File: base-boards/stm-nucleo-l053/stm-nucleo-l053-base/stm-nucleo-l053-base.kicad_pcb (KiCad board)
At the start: 2 copper layers, 162.6 x 104.8 mm, 18 parts, among them SW1 SW_SPST, SW2 SW_SPST, SW3 SW_SPST, SW4 SW_SPST, U1 NUCLEO-L053R8

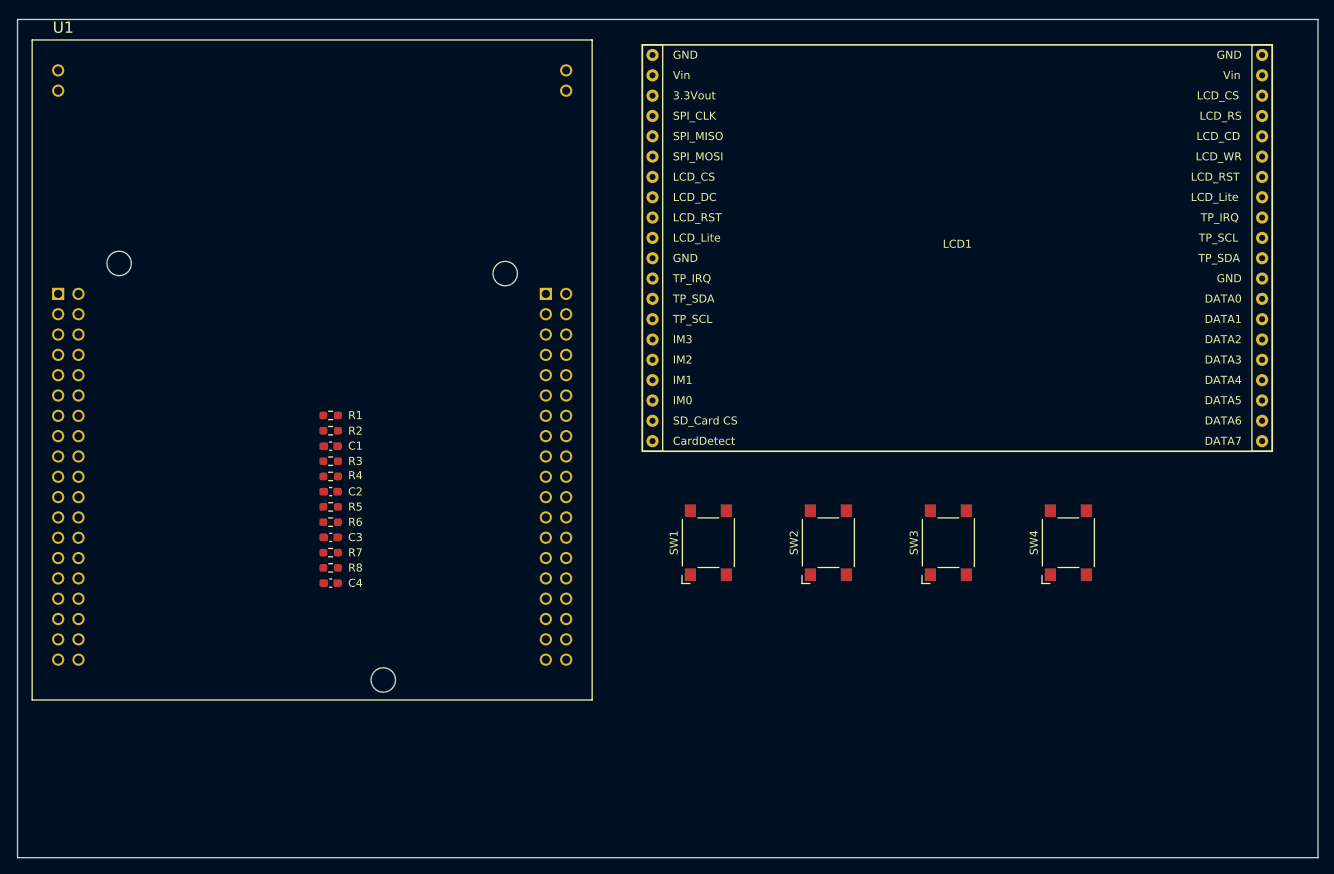
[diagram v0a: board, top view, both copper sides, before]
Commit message: Added Arduino Nano breakout
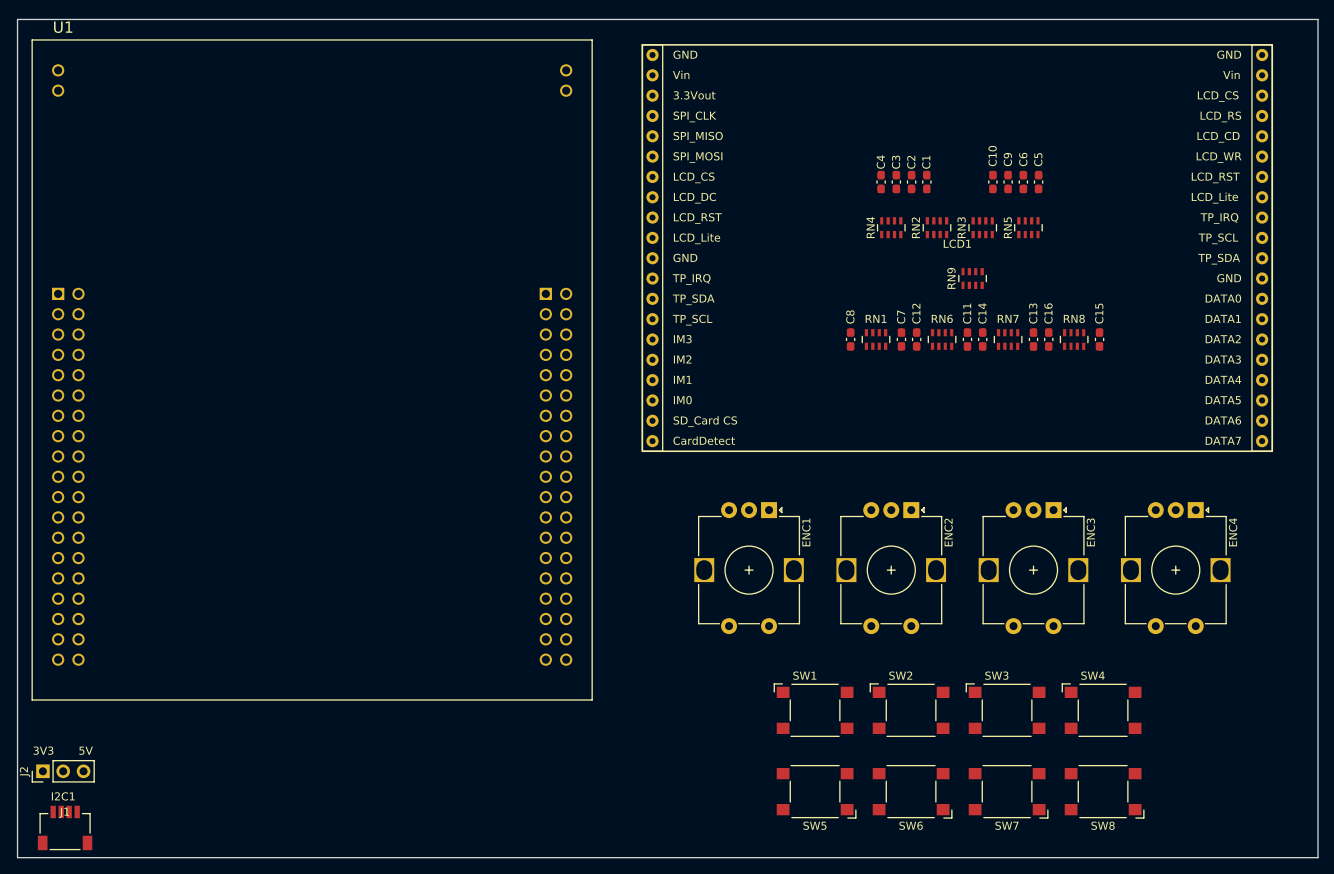
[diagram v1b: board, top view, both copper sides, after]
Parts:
- removed R1, R3, R5, R7: 10K, Resistor_SMD:R_0603_1608Metric_Pad0.98x0.95mm_HandSolder
- removed R2, R4, R6, R8: 1K, Resistor_SMD:R_0603_1608Metric_Pad0.98x0.95mm_HandSolder
- added C10: 10uF, Capacitor_SMD:C_0603_1608Metric_Pad1.08x0.95mm_HandSolder, F.Cu at (173.4, 61.0)
- added C11: 10nF, Capacitor_SMD:C_0603_1608Metric_Pad1.08x0.95mm_HandSolder, F.Cu at (170.2, 80.6)
- added C12: 10nF, Capacitor_SMD:C_0603_1608Metric_Pad1.08x0.95mm_HandSolder, F.Cu at (163.8, 80.6)
- added C13: 10nF, Capacitor_SMD:C_0603_1608Metric_Pad1.08x0.95mm_HandSolder, F.Cu at (178.4, 80.6)
- added C14: 10nF, Capacitor_SMD:C_0603_1608Metric_Pad1.08x0.95mm_HandSolder, F.Cu at (172.1, 80.6)
- added C15: 10nF, Capacitor_SMD:C_0603_1608Metric_Pad1.08x0.95mm_HandSolder, F.Cu at (186.7, 80.6)
- added C16: 10nF, Capacitor_SMD:C_0603_1608Metric_Pad1.08x0.95mm_HandSolder, F.Cu at (180.3, 80.6)
- added C5: 10uF, Capacitor_SMD:C_0603_1608Metric_Pad1.08x0.95mm_HandSolder, F.Cu at (179.1, 61.0)
- added C6: 10uF, Capacitor_SMD:C_0603_1608Metric_Pad1.08x0.95mm_HandSolder, F.Cu at (177.2, 61.0)
- added C7: 10nF, Capacitor_SMD:C_0603_1608Metric_Pad1.08x0.95mm_HandSolder, F.Cu at (161.9, 80.6)
- added C8: 10nF, Capacitor_SMD:C_0603_1608Metric_Pad1.08x0.95mm_HandSolder, F.Cu at (155.6, 80.6)
- added C9: 10uF, Capacitor_SMD:C_0603_1608Metric_Pad1.08x0.95mm_HandSolder, F.Cu at (175.3, 61.0)
- added ENC1: RotaryEncoder_Switch, Rotary_Encoder:RotaryEncoder_Alps_EC12E-Switch_Vertical_H20mm, F.Cu at (145.4, 102.0)
- added ENC2: RotaryEncoder_Switch, Rotary_Encoder:RotaryEncoder_Alps_EC12E-Switch_Vertical_H20mm, F.Cu at (163.2, 102.0)
- added ENC3: RotaryEncoder_Switch, Rotary_Encoder:RotaryEncoder_Alps_EC12E-Switch_Vertical_H20mm, F.Cu at (180.9, 102.0)
- added ENC4: RotaryEncoder_Switch, Rotary_Encoder:RotaryEncoder_Alps_EC12E-Switch_Vertical_H20mm, F.Cu at (198.7, 102.0)
- added J1: Qwiic-SM04B-SRSS-TBLFSN, KPM-Connectors:CONN_Qwiic_SM04B_JST, F.Cu at (55.9, 139.7)
- added J2: Conn_01x03, Connector_PinHeader_2.54mm:PinHeader_1x03_P2.54mm_Vertical, F.Cu at (54.6, 134.6)
- added RN1: 10k_Parallel, Resistor_SMD:R_Array_Concave_4x0603, F.Cu at (158.8, 80.6)
- added RN2: 10k_Parallel, Resistor_SMD:R_Array_Concave_4x0603, F.Cu at (166.4, 66.7)
- added RN3: 10k_Parallel, Resistor_SMD:R_Array_Concave_4x0603, F.Cu at (172.1, 66.7)
- added RN4: 1k_Parallel, Resistor_SMD:R_Array_Concave_4x0603, F.Cu at (160.7, 66.7)
- added RN5: 1k_Parallel, Resistor_SMD:R_Array_Concave_4x0603, F.Cu at (177.8, 66.7)
- added RN6: 10k_Parallel, Resistor_SMD:R_Array_Concave_4x0603, F.Cu at (167.0, 80.6)
- added RN7: 10k_Parallel, Resistor_SMD:R_Array_Concave_4x0603, F.Cu at (175.3, 80.6)
- added RN8: 10k_Parallel, Resistor_SMD:R_Array_Concave_4x0603, F.Cu at (183.5, 80.6)
- added RN9: 4k7_Parallel, Resistor_SMD:R_Array_Concave_4x0603, F.Cu at (170.8, 73.0)
- added SW5: SW_SPST, Button_Switch_SMD:SW_SPST_Omron_B3FS-101xP, F.Cu at (151.1, 137.2)
- added SW6: SW_SPST, Button_Switch_SMD:SW_SPST_Omron_B3FS-101xP, F.Cu at (163.1, 137.2)
- added SW7: SW_SPST, Button_Switch_SMD:SW_SPST_Omron_B3FS-101xP, F.Cu at (175.1, 137.2)
- added SW8: SW_SPST, Button_Switch_SMD:SW_SPST_Omron_B3FS-101xP, F.Cu at (187.1, 137.2)
- moved C4 85.1 mm to (159.4, 61.0), turned to -90 degrees
- moved C3 83.5 mm to (161.3, 61.0), turned to -90 degrees
- moved C2 82.3 mm to (163.2, 61.0), turned to -90 degrees
- moved C1 81.5 mm to (165.1, 61.0), turned to -90 degrees
- moved SW1 24.8 mm to (151.1, 127.0), turned to 0 degrees
- moved SW2 23.4 mm to (163.1, 127.0), turned to 0 degrees
- moved SW3 22.2 mm to (175.1, 127.0), turned to 0 degrees
- moved SW4 21.4 mm to (187.1, 127.0), turned to 0 degrees
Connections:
- LCD1 pad 13: unconnected-(LCD1-TP_SDA-Pad13) -> I2C1_SDA
- LCD1 pad 14: unconnected-(LCD1-TP_SCL-Pad14) -> I2C1_SCL
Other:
- board text added: "3V3"
- board text added: "5V"
- board text added: "I2C1"
